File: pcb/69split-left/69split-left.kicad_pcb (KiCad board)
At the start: 2 copper layers, 289.4 x 105.4 mm, 78 parts, among them J1 USB_C_Receptacle_USB2.0_14P, J2 Conn_02x03_Odd_Even, J3 USB_C_Receptacle, SW1 SW_Push, SW10 Q, SW11 W, SW12 E, SW13 R, SW14 T, SW15 Caps Lock, SW16 A, SW17 S, SW18 D, SW19 F, SW2 Esc, SW20 G, SW21 Shift, SW22 Z, SW23 X, SW24 C, SW25 V, SW26 B, SW27 Ctrl, SW28 Win, SW29 Alt, SW3 !,1,,F1, SW30 Space, SW4 @,2,,F2, SW5 #,3,,F3, SW6 $,4,,F4, SW7 %,5,,F5, SW8 ^,6,,F6, SW9 Tab, U1 ATmega32U4-AU, Y1 Crystal

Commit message: Started layout?
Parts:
- added D30: D, Diode_SMD:D_0805_2012Metric_Pad1.15x1.40mm_HandSolder, F.Cu at (47.3, 57.1)
- added D31: D, Diode_SMD:D_0805_2012Metric_Pad1.15x1.40mm_HandSolder, F.Cu at (47.3, 60.2)
- added NT1: NetTie_2, NetTie:NetTie-2_SMD_Pad0.5mm, F.Cu at (249.6, 122.9)
- added R10: 5k1, Resistor_SMD:R_0603_1608Metric_Pad0.98x0.95mm_HandSolder, F.Cu at (256.9, 121.9)
- added R11: 5k1, Resistor_SMD:R_0603_1608Metric_Pad0.98x0.95mm_HandSolder, F.Cu at (256.9, 124.4)
- added R7: 330R, Resistor_SMD:R_0603_1608Metric_Pad0.98x0.95mm_HandSolder, F.Cu at (250.6, 113.8)
- added R8: 22R, Resistor_SMD:R_0603_1608Metric_Pad0.98x0.95mm_HandSolder, F.Cu at (250.6, 116.3)
- added R9: 22R, Resistor_SMD:R_0603_1608Metric_Pad0.98x0.95mm_HandSolder, F.Cu at (250.6, 118.9)
- C1: value 10u -> 1u; footprint Capacitor_SMD:C_0805_2012Metric_Pad1.18x1.45mm_HandSolder -> Capacitor_SMD:C_0603_1608Metric_Pad1.08x0.95mm_HandSolder
- C5: value 1u -> 30p
- C7: value 30p -> 1u
- C8: value 1u -> 10u; footprint Capacitor_SMD:C_0603_1608Metric_Pad1.08x0.95mm_HandSolder -> Capacitor_SMD:C_0805_2012Metric_Pad1.18x1.45mm_HandSolder
- D1: value D -> Yellow LED; footprint Diode_SMD:D_0805_2012Metric_Pad1.15x1.40mm_HandSolder -> LED_SMD:LED_0805_2012Metric_Pad1.15x1.40mm_HandSolder
- D2: value D -> Blue LED; footprint Diode_SMD:D_0805_2012Metric_Pad1.15x1.40mm_HandSolder -> LED_SMD:LED_0805_2012Metric_Pad1.15x1.40mm_HandSolder
- D25, D26, D27, U1, Y1: moved to B.Cu
- J1: value USB_C_Receptacle_USB2.0_14P -> Conn_02x03_Odd_Even; footprint Connector_USB:USB_C_Receptacle_JAE_DX07S016JA1R1500 -> Connector_PinHeader_2.54mm:PinHeader_2x03_P2.54mm_Vertical
- J2: value Conn_02x03_Odd_Even -> USB_C_Receptacle; footprint Connector_PinHeader_2.54mm:PinHeader_2x03_P2.54mm_Vertical -> Connector_USB:USB_C_Receptacle_Amphenol_12401610E4-2A; moved to B.Cu
- J3: value USB_C_Receptacle -> USB_C_Receptacle_USB2.0_14P; footprint Connector_USB:USB_C_Receptacle_Amphenol_12401548E4-2A -> Connector_USB:USB_C_Receptacle_JAE_DX07S016JA1R1500; moved to B.Cu
- R1: value 22R -> 10k
- R2: value 22R -> 330R
- R3, R4: value 5k1 -> 330R
- R6: value 10k -> 330R
- SW30: footprint Button_Switch_Keyboard:SW_Cherry_MX_2.75u_PCB -> PCM_Switch_Keyboard_Cherry_MX:SW_Cherry_MX_PCB_3.00u
- moved D14 235.0 mm to (37.7, 69.3)
- moved D28 231.7 mm to (47.3, 51.1)
- moved D29 231.7 mm to (47.3, 54.1)
- moved D15 231.3 mm to (42.5, 51.1)
- moved D22 231.3 mm to (42.5, 54.1)
- moved D23 231.3 mm to (42.5, 57.1)
- moved D24 231.3 mm to (42.5, 60.2)
- moved D10 231.1 mm to (37.7, 57.1)
- moved D11 231.1 mm to (37.7, 60.2)
- moved D12 231.1 mm to (37.7, 63.2)
- moved D13 231.1 mm to (37.7, 66.3)
- moved D8 231.1 mm to (37.7, 51.1)
- moved D9 231.1 mm to (37.7, 54.1)
- moved J3 198.9 mm to (85.0, 41.5)
- moved D21 138.3 mm to (63.3, 56.7)
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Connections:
- C4 pad 1: VCC -> /ATmega32U4/RESET
- C5 pad 1: Net-(U1-~{RESET}) -> Net-(U1-XTAL1)
- C6 pad 1: Net-(U1-XTAL1) -> Net-(U1-XTAL2)
- C7 pad 1: Net-(U1-XTAL2) -> Net-(U1-UCAP)
- C8 pad 1: Net-(U1-UCAP) -> /ATmega32U4/VBUS
- D1 pad 1: (no net) -> GND
- D1 pad 2: (no net) -> Net-(D1-A)
- D10 pad 1: /69split Left Keyboard/ATmega32U4/ROW1 -> /ATmega32U4/ROW1
- D11 pad 1: /69split Left Keyboard/ATmega32U4/ROW1 -> /ATmega32U4/ROW1
- D12 pad 1: /69split Left Keyboard/ATmega32U4/ROW1 -> /ATmega32U4/ROW1
- D13 pad 1: /69split Left Keyboard/ATmega32U4/ROW1 -> /ATmega32U4/ROW1
- D14 pad 1: /69split Left Keyboard/ATmega32U4/ROW2 -> /ATmega32U4/ROW1
- D15 pad 1: /69split Left Keyboard/ATmega32U4/ROW2 -> /ATmega32U4/ROW1
- D16 pad 1: /69split Left Keyboard/ATmega32U4/ROW2 -> /ATmega32U4/ROW2
- D16 pad 2: (no net) -> Net-(D16-A)
- D17 pad 1: /69split Left Keyboard/ATmega32U4/ROW2 -> /ATmega32U4/ROW2
- D17 pad 2: (no net) -> Net-(D17-A)
- D18 pad 1: /69split Left Keyboard/ATmega32U4/ROW2 -> /ATmega32U4/ROW2
- D18 pad 2: (no net) -> Net-(D18-A)
- D19 pad 1: /69split Left Keyboard/ATmega32U4/ROW2 -> /ATmega32U4/ROW2
- D19 pad 2: (no net) -> Net-(D19-A)
- D2 pad 1: /69split Left Keyboard/ATmega32U4/ROW0 -> GND
- D2 pad 2: (no net) -> Net-(D2-A)
- D20 pad 1: (no net) -> /ATmega32U4/ROW2
- D20 pad 2: (no net) -> Net-(D20-A)
- D21 pad 1: /69split Left Keyboard/ATmega32U4/ROW3 -> /ATmega32U4/ROW2
- D21 pad 2: (no net) -> Net-(D21-A)
- D22 pad 1: /69split Left Keyboard/ATmega32U4/ROW3 -> /ATmega32U4/ROW3
- D23 pad 1: /69split Left Keyboard/ATmega32U4/ROW3 -> /ATmega32U4/ROW3
- D24 pad 1: /69split Left Keyboard/ATmega32U4/ROW3 -> /ATmega32U4/ROW3
- D25 pad 1: /69split Left Keyboard/ATmega32U4/ROW3 -> /ATmega32U4/ROW3
- D26 pad 1: /69split Left Keyboard/ATmega32U4/ROW4 -> /ATmega32U4/ROW3
- D27 pad 1: /69split Left Keyboard/ATmega32U4/ROW4 -> /ATmega32U4/ROW3
- D28 pad 1: /69split Left Keyboard/ATmega32U4/ROW4 -> /ATmega32U4/ROW4
- D29 pad 1: /69split Left Keyboard/ATmega32U4/ROW4 -> /ATmega32U4/ROW4
- D3 pad 1: /69split Left Keyboard/ATmega32U4/ROW0 -> /ATmega32U4/ROW0
- D3 pad 2: (no net) -> Net-(D3-A)
- D4 pad 1: /69split Left Keyboard/ATmega32U4/ROW0 -> /ATmega32U4/ROW0
- D4 pad 2: (no net) -> Net-(D4-A)
- D5 pad 1: /69split Left Keyboard/ATmega32U4/ROW0 -> /ATmega32U4/ROW0
- D5 pad 2: (no net) -> Net-(D5-A)
- D6 pad 1: /69split Left Keyboard/ATmega32U4/ROW0 -> /ATmega32U4/ROW0
- D6 pad 2: (no net) -> Net-(D6-A)
- D7 pad 1: /69split Left Keyboard/ATmega32U4/ROW0 -> /ATmega32U4/ROW0
- D7 pad 2: (no net) -> Net-(D7-A)
- D8 pad 1: /69split Left Keyboard/ATmega32U4/ROW1 -> /ATmega32U4/ROW0
- D9 pad 1: /69split Left Keyboard/ATmega32U4/ROW1 -> /ATmega32U4/ROW0
- J3 pad A4: /69split Left Keyboard/ATmega32U4/ROW0 -> VCC
- J3 pad A5: /69split Left Keyboard/ATmega32U4/ROW1 -> Net-(J3-CC1)
- J3 pad A6: /69split Left Keyboard/ATmega32U4/COL6 -> Net-(J3-D+-PadA6)
- J3 pad A7: /69split Left Keyboard/ATmega32U4/ROW3 -> Net-(J3-D--PadA7)
- J3 pad A8: unconnected-(J3-SBU1-PadA8) -> (no net)
- J3 pad A9: /69split Left Keyboard/ATmega32U4/ROW0 -> VCC
- J3 pad B4: /69split Left Keyboard/ATmega32U4/ROW0 -> VCC
- J3 pad B5: /69split Left Keyboard/ATmega32U4/ROW2 -> Net-(J3-CC2)
- J3 pad B6: /69split Left Keyboard/ATmega32U4/COL7 -> Net-(J3-D+-PadA6)
- J3 pad B7: /69split Left Keyboard/ATmega32U4/ROW4 -> Net-(J3-D--PadA7)
- J3 pad B8: unconnected-(J3-SBU2-PadB8) -> (no net)
- J3 pad B9: /69split Left Keyboard/ATmega32U4/ROW0 -> VCC
- R1 pad 1: /69split Left Keyboard/ATmega32U4/D- -> /ATmega32U4/RESET
- R1 pad 2: Net-(J1-D--PadA7) -> VCC
- R2 pad 1: /69split Left Keyboard/ATmega32U4/D+ -> /ATmega32U4/GPIO_OUT_PB5
- R2 pad 2: Net-(J1-D+-PadA6) -> Net-(U1-PB5)
- R3 pad 1: Net-(J1-CC2) -> /ATmega32U4/GPIO_OUT_PB6
- R3 pad 2: GND -> Net-(U1-PB6)
- R4 pad 1: Net-(J1-CC1) -> /ATmega32U4/GPIO_OUT_PB7
- R4 pad 2: GND -> Net-(U1-PB7)
- R5 pad 1: Net-(U1-~{RESET}) -> GND
- R5 pad 2: VCC -> Net-(U1-~{HWB}/PE2)
- R6 pad 1: GND -> Net-(D1-A)
- R6 pad 2: Net-(U1-~{HWB}/PE2) -> /ATmega32U4/INDICATOR_CAPS_LOCK
- SW1 pad 2: Net-(U1-~{RESET}) -> /ATmega32U4/RESET
- SW10 pad 1: /69split Left Keyboard/ATmega32U4/COL1 -> /ATmega32U4/COL1
- SW10 pad 2: Net-(D9-A) -> Net-(D11-A)
- SW11 pad 1: /69split Left Keyboard/ATmega32U4/COL2 -> /ATmega32U4/COL2
- SW11 pad 2: Net-(D10-A) -> Net-(D12-A)
- SW12 pad 1: /69split Left Keyboard/ATmega32U4/COL3 -> /ATmega32U4/COL3
- SW12 pad 2: Net-(D11-A) -> Net-(D13-A)
- SW13 pad 1: /69split Left Keyboard/ATmega32U4/COL4 -> /ATmega32U4/COL4
- SW13 pad 2: Net-(D12-A) -> Net-(D14-A)
- SW14 pad 1: /69split Left Keyboard/ATmega32U4/COL5 -> /ATmega32U4/COL5
- SW14 pad 2: Net-(D13-A) -> Net-(D15-A)
- SW15 pad 1: /69split Left Keyboard/ATmega32U4/COL0 -> /ATmega32U4/COL0
- SW15 pad 2: Net-(D14-A) -> Net-(D16-A)
- SW16 pad 1: /69split Left Keyboard/ATmega32U4/COL1 -> /ATmega32U4/COL1
- SW16 pad 2: Net-(D15-A) -> Net-(D17-A)
- SW17 pad 1: /69split Left Keyboard/ATmega32U4/COL2 -> /ATmega32U4/COL2
- SW17 pad 2: Net-(D16-A) -> Net-(D18-A)
- SW18 pad 1: /69split Left Keyboard/ATmega32U4/COL3 -> /ATmega32U4/COL3
- SW18 pad 2: Net-(D17-A) -> Net-(D19-A)
- SW19 pad 1: /69split Left Keyboard/ATmega32U4/COL4 -> /ATmega32U4/COL4
- SW19 pad 2: Net-(D18-A) -> Net-(D20-A)
- SW2 pad 1: (no net) -> /ATmega32U4/COL0
- SW2 pad 2: Net-(D1-A) -> Net-(D3-A)
- SW20 pad 1: /69split Left Keyboard/ATmega32U4/COL5 -> /ATmega32U4/COL5
- SW20 pad 2: Net-(D19-A) -> Net-(D21-A)
- SW21 pad 1: /69split Left Keyboard/ATmega32U4/COL0 -> /ATmega32U4/COL0
- SW21 pad 2: Net-(D20-A) -> Net-(D22-A)
- SW22 pad 1: /69split Left Keyboard/ATmega32U4/COL1 -> /ATmega32U4/COL1
- SW22 pad 2: Net-(D21-A) -> Net-(D23-A)
- SW23 pad 1: /69split Left Keyboard/ATmega32U4/COL2 -> /ATmega32U4/COL2
- SW23 pad 2: Net-(D22-A) -> Net-(D24-A)
- SW24 pad 1: /69split Left Keyboard/ATmega32U4/COL3 -> /ATmega32U4/COL3
- SW24 pad 2: Net-(D23-A) -> Net-(D25-A)
- SW25 pad 1: /69split Left Keyboard/ATmega32U4/COL4 -> /ATmega32U4/COL4
- SW25 pad 2: Net-(D24-A) -> Net-(D26-A)
- SW26 pad 1: /69split Left Keyboard/ATmega32U4/COL5 -> /ATmega32U4/COL5
- SW26 pad 2: Net-(D25-A) -> Net-(D27-A)
- SW27 pad 1: /69split Left Keyboard/ATmega32U4/COL0 -> /ATmega32U4/COL0
- SW27 pad 2: Net-(D26-A) -> Net-(D28-A)
- SW28 pad 1: /69split Left Keyboard/ATmega32U4/COL1 -> /ATmega32U4/COL1
- SW28 pad 2: Net-(D27-A) -> Net-(D29-A)
- SW29 pad 1: /69split Left Keyboard/ATmega32U4/COL2 -> /ATmega32U4/COL2
- SW29 pad 2: Net-(D28-A) -> Net-(D30-A)
- SW3 pad 1: /69split Left Keyboard/ATmega32U4/COL1 -> /ATmega32U4/COL1
- SW3 pad 2: Net-(D2-A) -> Net-(D4-A)
- SW30 pad 1: /69split Left Keyboard/ATmega32U4/COL3 -> /ATmega32U4/COL3
- SW30 pad 2: Net-(D29-A) -> Net-(D31-A)
- SW4 pad 1: /69split Left Keyboard/ATmega32U4/COL2 -> /ATmega32U4/COL2
- SW4 pad 2: Net-(D3-A) -> Net-(D5-A)
- SW5 pad 1: /69split Left Keyboard/ATmega32U4/COL3 -> /ATmega32U4/COL3
- SW5 pad 2: Net-(D4-A) -> Net-(D6-A)
- SW6 pad 1: (no net) -> /ATmega32U4/COL4
- SW6 pad 2: Net-(D5-A) -> Net-(D7-A)
- SW7 pad 1: (no net) -> /ATmega32U4/COL5
- SW7 pad 2: Net-(D6-A) -> Net-(D8-A)
- SW8 pad 1: /69split Left Keyboard/ATmega32U4/COL6 -> /ATmega32U4/COL6
- SW8 pad 2: Net-(D7-A) -> Net-(D9-A)
- SW9 pad 1: /69split Left Keyboard/ATmega32U4/COL0 -> /ATmega32U4/COL0
- SW9 pad 2: Net-(D8-A) -> Net-(D10-A)
- U1 pad 1: unconnected-(U1-PE6-Pad1) -> /ATmega32U4/INDICATOR_GPIO
- U1 pad 10: /69split Left Keyboard/ATmega32U4/COL2 -> /ATmega32U4/ROW1
- U1 pad 11: /69split Left Keyboard/ATmega32U4/COL3 -> /ATmega32U4/ROW2
- U1 pad 12: /69split Left Keyboard/ATmega32U4/COL4 -> Net-(U1-PB7)
- U1 pad 13: Net-(U1-~{RESET}) -> /ATmega32U4/RESET
- U1 pad 18: /69split Left Keyboard/ATmega32U4/COL5 -> /ATmega32U4/ROW3
- U1 pad 19: /69split Left Keyboard/ATmega32U4/COL6 -> /ATmega32U4/ROW4
- U1 pad 20: /69split Left Keyboard/ATmega32U4/COL7 -> /ATmega32U4/COL0
- U1 pad 21: /69split Left Keyboard/ATmega32U4/COL8 -> /ATmega32U4/COL1
- U1 pad 22: /69split Left Keyboard/ATmega32U4/COL9 -> /ATmega32U4/COL3
- U1 pad 25: /69split Left Keyboard/ATmega32U4/COL10 -> /ATmega32U4/COL2
- U1 pad 26: unconnected-(U1-PD6-Pad26) -> /ATmega32U4/COL4
- U1 pad 27: unconnected-(U1-PD7-Pad27) -> /ATmega32U4/COL5
- U1 pad 28: /69split Left Keyboard/ATmega32U4/ROW4 -> /ATmega32U4/COL6
- U1 pad 29: /69split Left Keyboard/ATmega32U4/ROW3 -> Net-(U1-PB5)
- U1 pad 3: /69split Left Keyboard/ATmega32U4/D- -> /ATmega32U4/D-
- U1 pad 30: /69split Left Keyboard/ATmega32U4/ROW2 -> Net-(U1-PB6)
- U1 pad 31: /69split Left Keyboard/ATmega32U4/ROW1 -> /ATmega32U4/COL7
- U1 pad 32: /69split Left Keyboard/ATmega32U4/ROW0 -> /ATmega32U4/COL8
- U1 pad 36: /69split Left Keyboard/ATmega32U4/COL11 -> /ATmega32U4/COL9
- U1 pad 37: /69split Left Keyboard/ATmega32U4/COL12 -> /ATmega32U4/COL10
- U1 pad 38: /69split Left Keyboard/ATmega32U4/COL13 -> /ATmega32U4/COL11
- U1 pad 39: /69split Left Keyboard/ATmega32U4/COL14 -> /ATmega32U4/COL12
- U1 pad 4: /69split Left Keyboard/ATmega32U4/D+ -> /ATmega32U4/D+
- U1 pad 40: unconnected-(U1-PF1-Pad40) -> /ATmega32U4/COL13
- U1 pad 41: unconnected-(U1-PF0-Pad41) -> /ATmega32U4/COL14
- U1 pad 7: VCC -> /ATmega32U4/VBUS
- U1 pad 8: /69split Left Keyboard/ATmega32U4/COL0 -> /ATmega32U4/INDICATOR_CAPS_LOCK
- U1 pad 9: /69split Left Keyboard/ATmega32U4/COL1 -> /ATmega32U4/ROW0

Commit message: Continued layout.
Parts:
- removed NT1: NetTie_2, NetTie:NetTie-2_SMD_Pad0.5mm
- removed R2, R3, R4: 330R, Resistor_SMD:R_0603_1608Metric_Pad0.98x0.95mm_HandSolder
- added C9: 1u, Capacitor_SMD:C_0603_1608Metric_Pad1.08x0.95mm_HandSolder, B.Cu at (108.3, 110.3)
- C1, C2, C3, C4, C5, C6, C7, R1, R10, R11, R5, R8, R9: moved to B.Cu
- C8: footprint Capacitor_SMD:C_0805_2012Metric_Pad1.18x1.45mm_HandSolder -> Capacitor_SMD:C_0603_1608Metric_Pad1.08x0.95mm_HandSolder; moved to B.Cu
- D1, D2: moved to F.Cu
- D10, D11, D12, D13, D14, D15, D22, D23, D24, D28, D29, D30, D31, D8, D9: footprint Diode_SMD:D_0805_2012Metric_Pad1.15x1.40mm_HandSolder -> Diode_THT:D_DO-35_SOD27_P7.62mm_Horizontal
- D16, D17, D18, D19, D20, D21, D25, D26, D27, D3, D4, D5, D6, D7: footprint Diode_SMD:D_0805_2012Metric_Pad1.15x1.40mm_HandSolder -> Diode_THT:D_DO-35_SOD27_P7.62mm_Horizontal; moved to F.Cu
- J2: footprint Connector_USB:USB_C_Receptacle_Amphenol_12401610E4-2A -> Connector_USB:USB_C_Receptacle_Amphenol_12401548E4-2A
- SW21: footprint Button_Switch_Keyboard:SW_Cherry_MX_2.25u_PCB -> PCM_Switch_Keyboard_Cherry_MX:SW_Cherry_MX_PCB_2.25u
- moved R11 185.5 mm to (90.1, 43.3), turned to 90 degrees
- moved R6 179.7 mm to (76.8, 90.4), turned to -90 degrees
- moved D9 176.9 mm to (214.5, 57.0), turned to 90 degrees
- moved R10 174.0 mm to (100.0, 46.7)
- moved C8 169.9 mm to (94.5, 46.7), turned to 180 degrees
- moved R8 164.8 mm to (96.8, 57.1), turned to 90 degrees
- moved R9 164.0 mm to (98.6, 57.1), turned to 90 degrees
- moved C1 151.0 mm to (121.2, 98.7)
- moved R5 150.4 mm to (105.5, 101.2), turned to 90 degrees
- moved C2 148.1 mm to (108.7, 101.2), turned to -90 degrees
- moved D8 145.2 mm to (182.5, 40.5), turned to 180 degrees
- moved D31 144.0 mm to (171.4, 133.1), turned to 90 degrees
- moved D15 143.8 mm to (184.1, 76.2), turned to 90 degrees
- moved C5 141.8 mm to (115.7, 114.1)
- moved C6 138.1 mm to (119.1, 114.1)
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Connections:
- C8 pad 1: /ATmega32U4/VBUS -> VCC
- U1 pad 12: Net-(U1-PB7) -> /ATmega32U4/GPIO_OUT_PB7
- U1 pad 29: Net-(U1-PB5) -> /ATmega32U4/GPIO_OUT_PB5
- U1 pad 30: Net-(U1-PB6) -> /ATmega32U4/GPIO_OUT_PB6
- U1 pad 7: /ATmega32U4/VBUS -> VCC
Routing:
- net /ATmega32U4/COL3: track 0.00 -> 219.3 mm, vias 0 -> 1
- net VCC: track 0.00 -> 161.9 mm
- net /ATmega32U4/ROW0: track 0.00 -> 152.2 mm
- net /ATmega32U4/RESET: track 0.00 -> 140.3 mm
- net /ATmega32U4/ROW3: track 0.00 -> 134.5 mm
- net /ATmega32U4/COL1: track 0.00 -> 127.5 mm, vias 0 -> 1
- net /ATmega32U4/ROW4: track 0.00 -> 123.7 mm, vias 0 -> 1
- net /ATmega32U4/D+: track 0.00 -> 109.5 mm
- net /ATmega32U4/D-: track 0.00 -> 108.9 mm
- net /ATmega32U4/ROW2: track 0.00 -> 103.1 mm
- net /ATmega32U4/COL0: track 0.00 -> 101.5 mm, vias 0 -> 1
- net /ATmega32U4/ROW1: track 0.00 -> 100.3 mm
- net /ATmega32U4/COL2: track 0.00 -> 97.1 mm
- net /ATmega32U4/COL4: track 0.00 -> 72.8 mm
- net /ATmega32U4/COL5: track 0.00 -> 70.6 mm
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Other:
- board size 289.4 x 105.4 mm -> 143.3 x 105.4 mm

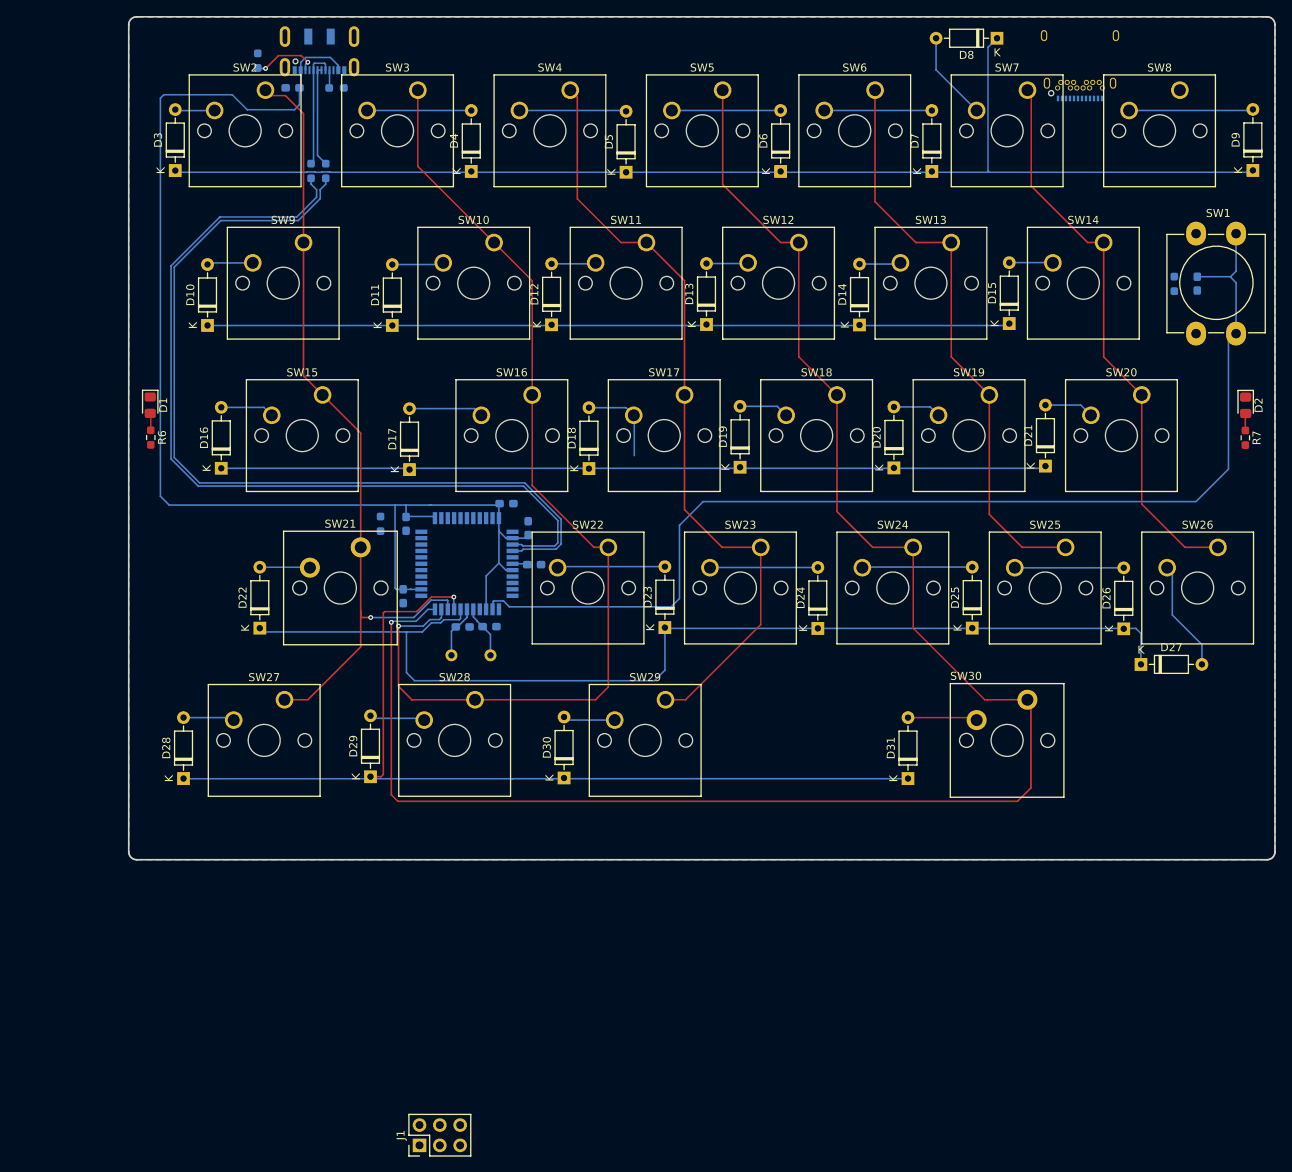
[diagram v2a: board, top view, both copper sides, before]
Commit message: Practically finished the left side - need to make a footprint for the split USB connector. Some other schematic changes were made that I will not list. I should've made more commits between ths one and the previous one but it is what it is.
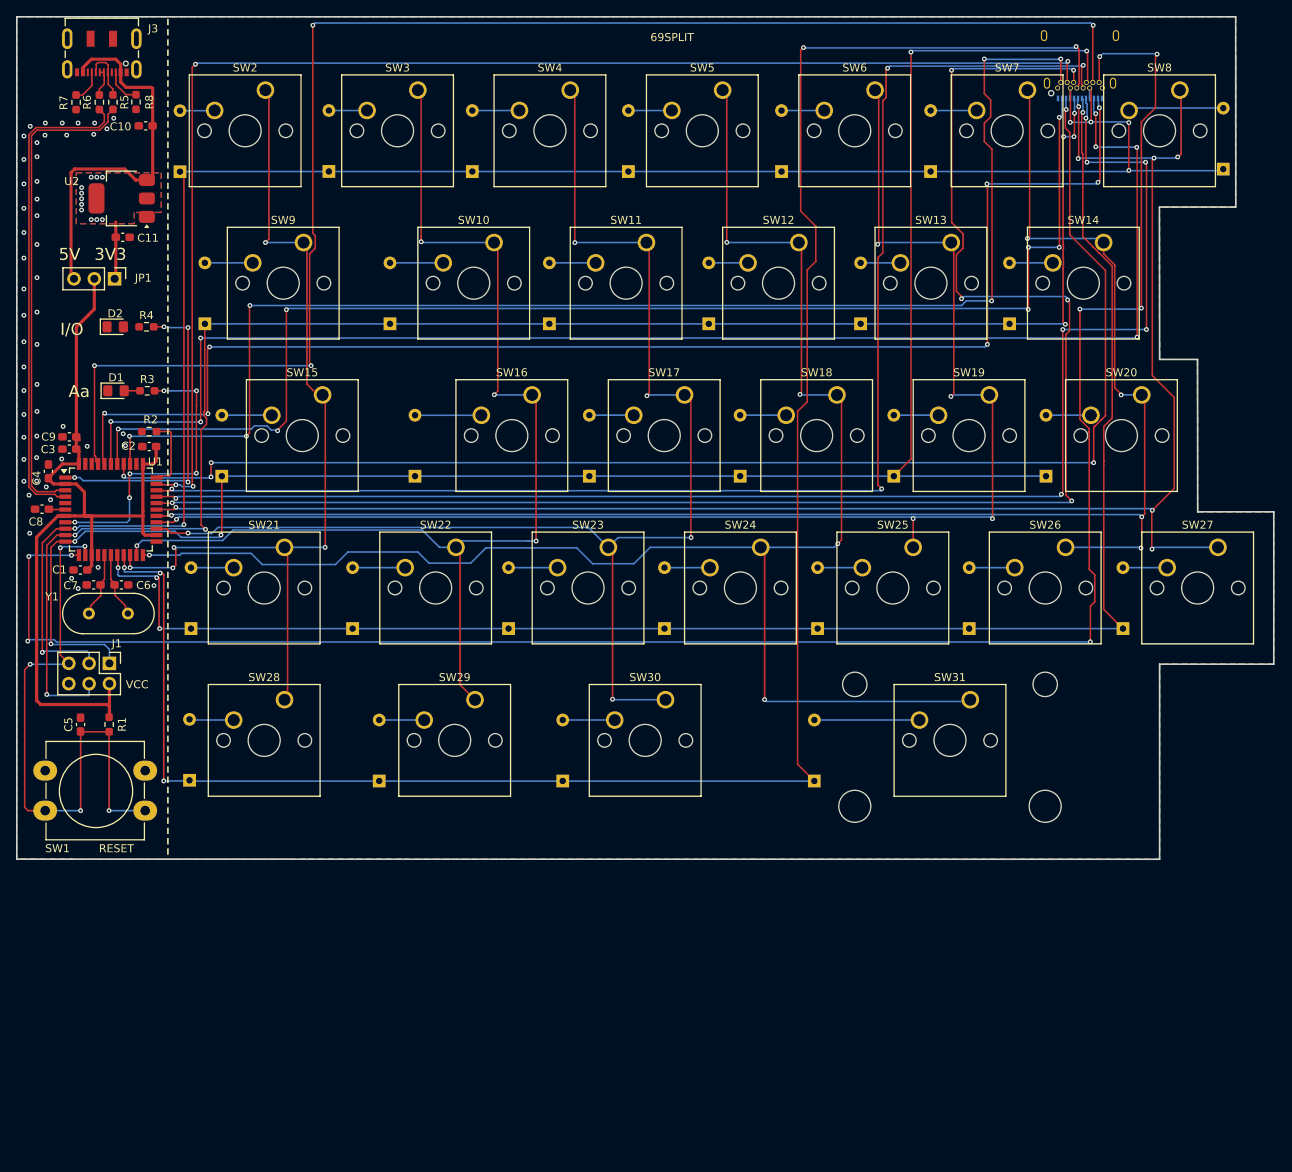
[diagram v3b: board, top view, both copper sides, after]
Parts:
- removed R10, R11: 5k1, Resistor_SMD:R_0603_1608Metric_Pad0.98x0.95mm_HandSolder
- removed R9: 22R, Resistor_SMD:R_0603_1608Metric_Pad0.98x0.95mm_HandSolder
- added C10: 1u, Capacitor_SMD:C_0603_1608Metric_Pad1.08x0.95mm_HandSolder, F.Cu at (76.1, 51.5)
- added C11: 2.2u, Capacitor_SMD:C_0603_1608Metric_Pad1.08x0.95mm_HandSolder, F.Cu at (73.2, 65.4)
- added D32: D, Diode_THT:D_DO-35_SOD27_P7.62mm_Horizontal, B.Cu at (159.7, 133.4)
- added JP1: Jumper_3_Bridged12, Connector_PinHeader_2.54mm:PinHeader_1x03_P2.54mm_Vertical, F.Cu at (72.2, 70.6)
- added R2: 10k, Resistor_SMD:R_0603_1608Metric_Pad0.98x0.95mm_HandSolder, F.Cu at (76.5, 89.7)
- added R3: 200R, Resistor_SMD:R_0603_1608Metric_Pad0.98x0.95mm_HandSolder, F.Cu at (76.3, 84.6)
- added R4: 200R, Resistor_SMD:R_0603_1608Metric_Pad0.98x0.95mm_HandSolder, F.Cu at (76.2, 76.6)
- added SW31: Space, Button_Switch_Keyboard:SW_Cherry_MX_2.75u_PCB, F.Cu at (179.2, 123.2)
- added U2: TLV76133DCY, Package_TO_SOT_SMD:SOT-223-3_TabPin2, F.Cu at (73.1, 60.6)
- C1, C2, C3, C4, C6, J3, R1, U1, Y1: moved to F.Cu
- C5: value 30p -> 1u; moved to F.Cu
- C7: value 1u -> 30p; moved to F.Cu
- C8: value 10u -> 1u; moved to F.Cu
- C9: value 1u -> 10u; moved to F.Cu
- D10, D11, D12, D13, D14, D15, D16, D17, D18, D19, D20, D21, D22, D23, D24, D25, D26, D27, D28, D29, D3, D30, D31, D4, D5, D6, D7, D8, D9: moved to B.Cu
- D2: value Blue LED -> Amber LED
- R5: value 10k -> 22R; moved to F.Cu
- R6: value 330R -> 22R
- R7: value 330R -> 5k1
- R8: value 22R -> 5k1; moved to F.Cu
- SW21: footprint PCM_Switch_Keyboard_Cherry_MX:SW_Cherry_MX_PCB_2.25u -> Button_Switch_Keyboard:SW_Cherry_MX_1.25u_PCB
- SW22: value Z -> \|
- SW23: value X -> Z
- SW24: value C -> X
- SW25: value V -> C
- SW26: value B -> V
- SW27: value Ctrl -> B; footprint Button_Switch_Keyboard:SW_Cherry_MX_1.25u_PCB -> Button_Switch_Keyboard:SW_Cherry_MX_1.00u_PCB
- SW28: value Win -> Ctrl
- SW29: value Alt -> Win
- SW30: value Space -> Alt; footprint PCM_Switch_Keyboard_Cherry_MX:SW_Cherry_MX_PCB_3.00u -> Button_Switch_Keyboard:SW_Cherry_MX_1.25u_PCB
- moved SW1 153.9 mm to (63.5, 132.1), turned to 0 degrees
- moved R7 152.1 mm to (67.4, 48.5)
- moved C4 145.5 mm to (64.0, 94.7), turned to 90 degrees
- moved R1 144.1 mm to (71.5, 126.3), turned to 90 degrees
- moved D2 141.7 mm to (72.3, 76.6), turned to 0 degrees
- moved D28 118.9 mm to (198.3, 114.3)
- moved SW27 118.2 mm to (210.1, 104.2)
- moved J1 71.6 mm to (71.6, 118.7), turned to -90 degrees
- moved R5 62.4 mm to (72.0, 48.5)
- moved C8 61.3 mm to (63.1, 99.4)
- moved C3 58.2 mm to (66.6, 91.9), turned to 180 degrees
- moved C7 55.1 mm to (69.6, 108.9), turned to 180 degrees
- moved C1 53.9 mm to (68.0, 107.0), turned to 180 degrees
- moved C5 49.3 mm to (68.0, 126.3), turned to 90 degrees
- moved C6 46.3 mm to (73.1, 108.9)
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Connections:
- C4 pad 1: /ATmega32U4/RESET -> VCC
- C5 pad 1: Net-(U1-XTAL1) -> /ATmega32U4/RESET
- C6 pad 1: Net-(U1-XTAL2) -> Net-(U1-XTAL1)
- C7 pad 1: Net-(U1-UCAP) -> Net-(U1-XTAL2)
- C8 pad 1: VCC -> Net-(U1-UCAP)
- C9 pad 1: VCC -> /LDO & Jumper/USB_5V
- D28 pad 1: /ATmega32U4/ROW4 -> /ATmega32U4/ROW3
- J1 pad 1: VCC -> /ATmega32U4/ROW2
- J1 pad 2: /ATmega32U4/COL3 -> VCC
- J1 pad 3: /ATmega32U4/COL2 -> /ATmega32U4/ROW0
- J1 pad 4: /ATmega32U4/COL1 -> /ATmega32U4/ROW1
- J1 pad 5: GND -> /ATmega32U4/RESET
- J1 pad 6: /ATmega32U4/RESET -> GND
- J3 pad A4: VCC -> /LDO & Jumper/USB_5V
- J3 pad A9: VCC -> /LDO & Jumper/USB_5V
- J3 pad B4: VCC -> /LDO & Jumper/USB_5V
- J3 pad B9: VCC -> /LDO & Jumper/USB_5V
- R5 pad 1: GND -> /ATmega32U4/D-
- R5 pad 2: Net-(U1-~{HWB}/PE2) -> Net-(J3-D--PadA7)
- R6 pad 1: Net-(D1-A) -> /ATmega32U4/D+
- R6 pad 2: /ATmega32U4/INDICATOR_CAPS_LOCK -> Net-(J3-D+-PadA6)
- R7 pad 1: Net-(D2-A) -> Net-(J3-CC2)
- R7 pad 2: /ATmega32U4/INDICATOR_GPIO -> GND
- R8 pad 1: /ATmega32U4/D- -> Net-(J3-CC1)
- R8 pad 2: Net-(J3-D--PadA7) -> GND
- SW27 pad 1: /ATmega32U4/COL0 -> /ATmega32U4/COL6
- SW28 pad 1: /ATmega32U4/COL1 -> /ATmega32U4/COL0
- SW29 pad 1: /ATmega32U4/COL2 -> /ATmega32U4/COL1
- SW30 pad 1: /ATmega32U4/COL3 -> /ATmega32U4/COL2
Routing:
- net /ATmega32U4/GPIO_OUT_PB7: track 0.00 -> 243.5 mm, vias 0 -> 8
- net /ATmega32U4/COL6: track 0.00 -> 213.2 mm, vias 0 -> 7
- net /ATmega32U4/GPIO_OUT_PB5: track 0.00 -> 200.6 mm, vias 0 -> 6
- net /ATmega32U4/COL14: track 0.00 -> 187.6 mm, vias 0 -> 4
- net /ATmega32U4/GPIO_OUT_PB6: track 0.00 -> 181.2 mm, vias 0 -> 7
- net /ATmega32U4/COL12: track 0.00 -> 179.3 mm, vias 0 -> 7
- net /ATmega32U4/COL10: track 0.00 -> 173.0 mm, vias 0 -> 5
- net /ATmega32U4/COL7: track 0.00 -> 171.9 mm, vias 0 -> 4
- net /ATmega32U4/COL9: track 0.00 -> 171.4 mm, vias 0 -> 6
- net /ATmega32U4/COL13: track 0.00 -> 170.1 mm, vias 0 -> 7
- net /ATmega32U4/COL8: track 0.00 -> 169.6 mm, vias 0 -> 4
- net /ATmega32U4/COL11: track 0.00 -> 163.7 mm, vias 0 -> 7
- net /ATmega32U4/COL5: track 70.6 -> 203.3 mm, vias 0 -> 5
- net /ATmega32U4/ROW2: track 103.1 -> 234.4 mm, vias 0 -> 5
- net /ATmega32U4/ROW4: track 123.7 -> 248.4 mm, vias 1 -> 5
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- added copper zone on B.Cu, net /LDO & Jumper/3V3
- added copper zone on F.Cu, net /LDO & Jumper/3V3
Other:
- board size 143.3 x 105.4 mm -> 157.1 x 105.3 mm
- board text added: "3V3"
- board text added: "5V"
- board text added: "69SPLIT"
- board text added: "Aa"
- board text added: "I/O"
- board text added: "RESET"
- board text added: "VCC"
